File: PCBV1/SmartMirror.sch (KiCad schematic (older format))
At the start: 0 parts

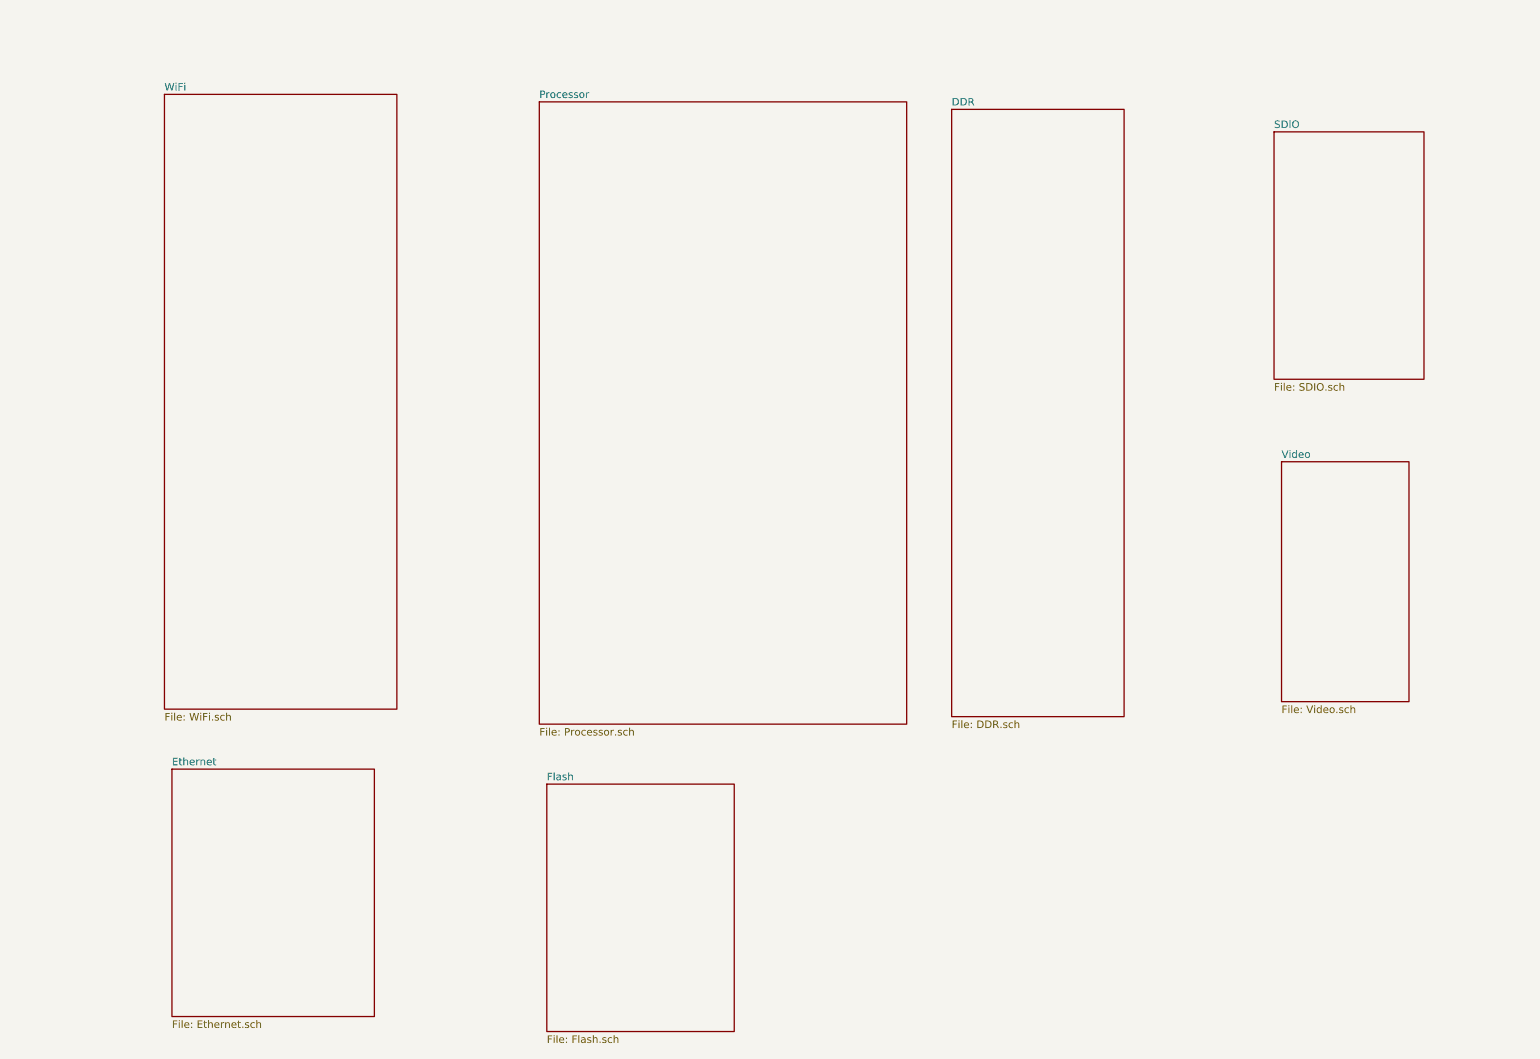
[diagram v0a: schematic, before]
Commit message: Added schematic for power through barrel jack and voltage converters, connected DRAM.
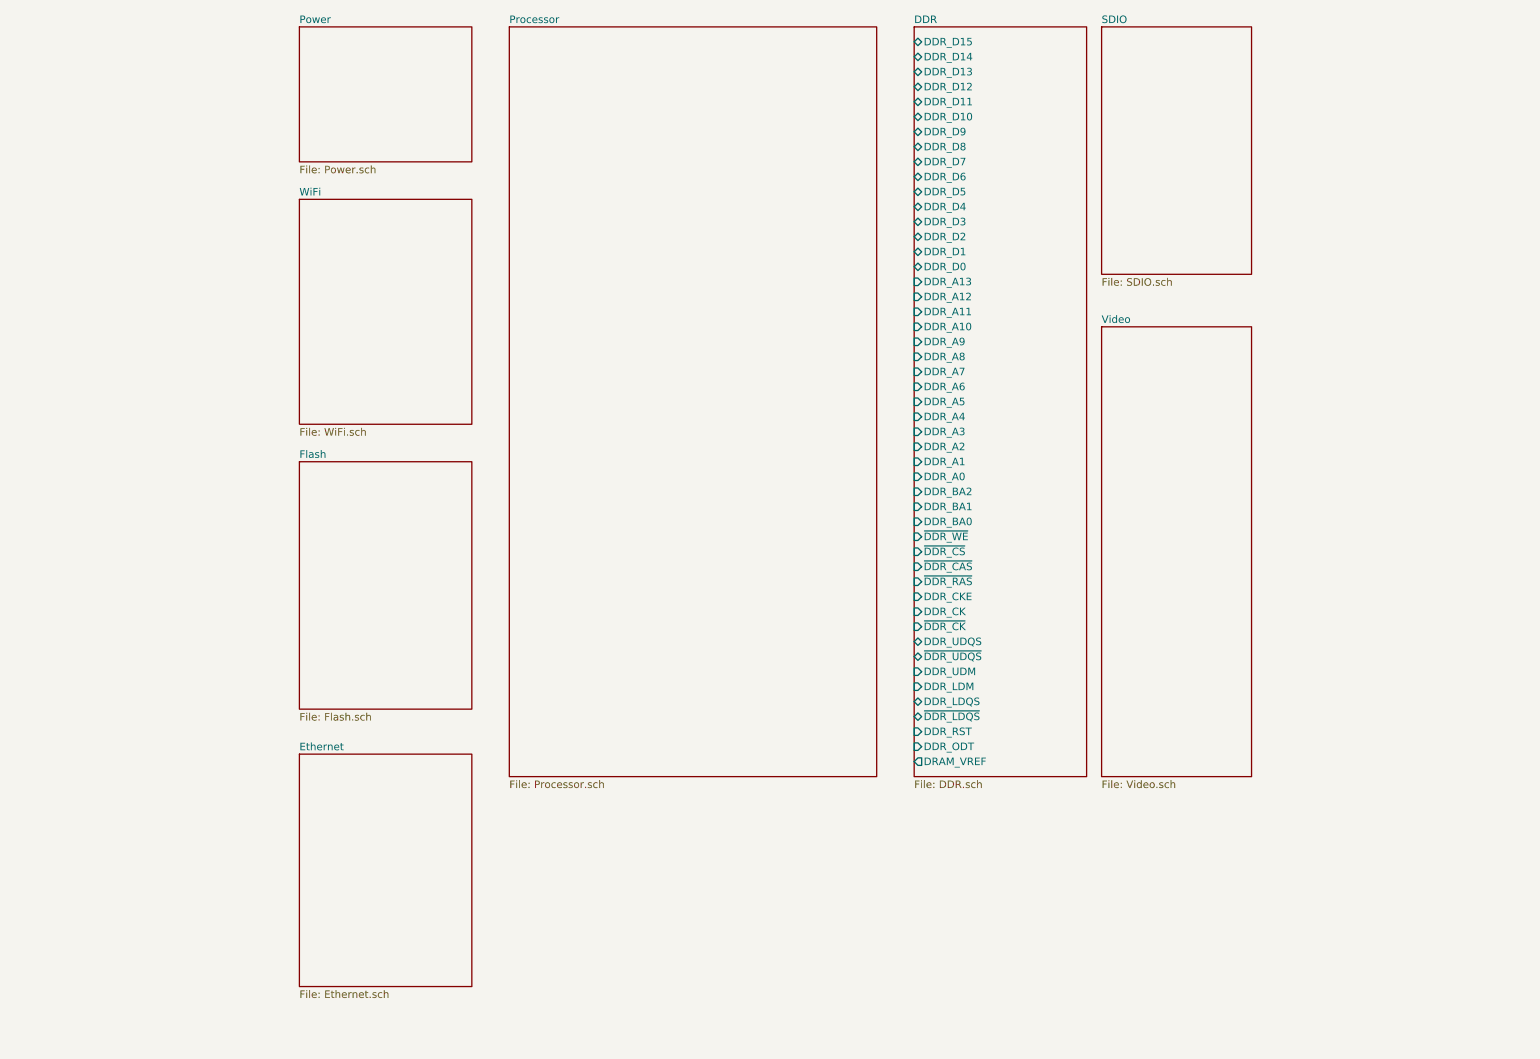
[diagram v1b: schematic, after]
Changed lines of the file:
@@
 $Descr A4 11693 8268
 encoding utf-8
-Sheet 1 8
+Sheet 1 9
 Title "Smart Mirror"
 Date "2021-01-21"
@@
 $EndDescr
 $Sheet
-S 4400 1350 2450 4150
+S 4200 850  2450 5000
 U 6009E1D9
 F0 "Processor" 50
@@
 $EndSheet
 $Sheet
-S 7150 1400 1150 4050
-U 6009E3C0
-F0 "DDR" 50
-F1 "DDR.sch" 50
-$EndSheet
-$Sheet
-S 1900 1300 1550 4100
+S 2800 2000 1150 1500
 U 6009E54D
 F0 "WiFi" 50
@@
 $EndSheet
 $Sheet
-S 1950 5800 1350 1650
+S 2800 5700 1150 1550
 U 6009E63D
 F0 "Ethernet" 50
@@
 $EndSheet
 $Sheet
-S 9300 1550 1000 1650
+S 8150 850  1000 1650
 U 6009E6CB
 F0 "SDIO" 50
@@
 $EndSheet
 $Sheet
-S 9350 3750 850  1600
+S 8150 2850 1000 3000
 U 6009E791
 F0 "Video" 50
@@
 $EndSheet
 $Sheet
-S 4450 5900 1250 1650
+S 2800 3750 1150 1650
 U 6009E7FD
 F0 "Flash" 50
 F1 "Flash.sch" 50
 $EndSheet
+$Sheet
+S 2800 850  1150 900
+U 60251FB2
+F0 "Power" 50
+F1 "Power.sch" 50
+$EndSheet
+$Sheet
+S 6900 850  1150 5000
+U 6009E3C0
+F0 "DDR" 50
+F1 "DDR.sch" 50
+F2 "DDR_D13" B L 6900 1150 50
+F3 "DDR_D15" B L 6900 950 50
+F4 "DDR_D12" B L 6900 1250 50
+F5 "DDR_D14" B L 6900 1050 50
+F6 "DDR_D11" B L 6900 1350 50
+F7 "DDR_D9" B L 6900 1550 50
+F8 "DDR_D10" B L 6900 1450 50
+F9 "DDR_D8" B L 6900 1650 50
+F10 "DDR_D0" B L 6900 2450 50
+F11 "DDR_D2" B L 6900 2250 50
+F12 "DDR_D1" B L 6900 2350 50
+F13 "DDR_D3" B L 6900 2150 50
+F14 "DDR_D6" B L 6900 1850 50
+F15 "DDR_D4" B L 6900 2050 50
+F16 "DDR_D7" B L 6900 1750 50
+F17 "DDR_D5" B L 6900 1950 50
+F18 "DDR_A8" I L 6900 3050 50
+F19 "DDR_A13" I L 6900 2550 50
+F20 "DDR_A6" I L 6900 3250 50
+F21 "DDR_A11" I L 6900 2750 50
+F22 "DDR_A9" I L 6900 2950 50
+F23 "DDR_A7" I L 6900 3150 50
+F24 "DDR_A4" I L 6900 3450 50
+F25 "DDR_A1" I L 6900 3750 50
+F26 "DDR_A2" I L 6900 3650 50
+F27 "DDR_A5" I L 6900 3350 50
+F28 "DDR_A0" I L 6900 3850 50
+F29 "DDR_A3" I L 6900 3550 50
+F30 "DDR_A12" I L 6900 2650 50
+F31 "DDR_A10" I L 6900 2850 50
+F32 "DDR_BA1" I L 6900 4050 50
+F33 "DDR_BA2" I L 6900 3950 50
+F34 "DDR_BA0" I L 6900 4150 50
+F35 "~DDR_WE" I L 6900 4250 50
+F36 "~DDR_CS" I L 6900 4350 50
+F37 "DDR_CKE" I L 6900 4650 50
+F38 "~DDR_CK" I L 6900 4850 50
+F39 "~DDR_CAS" I L 6900 4450 50
+F40 "DDR_CK" I L 6900 4750 50
+F41 "~DDR_RAS" I L 6900 4550 50
+F42 "~DDR_UDQS" B L 6900 5050 50
+F43 "DDR_UDQS" B L 6900 4950 50
+F44 "DDR_UDM" I L 6900 5150 50
+F45 "DDR_LDM" I L 6900 5250 50
+F46 "DDR_LDQS" B L 6900 5350 50
+F47 "~DDR_LDQS" B L 6900 5450 50
+F48 "DDR_RST" I L 6900 5550 50
+F49 "DDR_ODT" I L 6900 5650 50
+F50 "DRAM_VREF" O L 6900 5750 50
+$EndSheet
 $EndSCHEMATC

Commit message: Made comments and some circuits.
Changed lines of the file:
@@
 $Descr A4 11693 8268
 encoding utf-8
-Sheet 1 9
+Sheet 1 8
 Title "Smart Mirror"
 Date "2021-01-21"
@@
 $EndSheet
 $Sheet
-S 2800 5700 1150 1550
-U 6009E63D
-F0 "Ethernet" 50
-F1 "Ethernet.sch" 50
-$EndSheet
-$Sheet

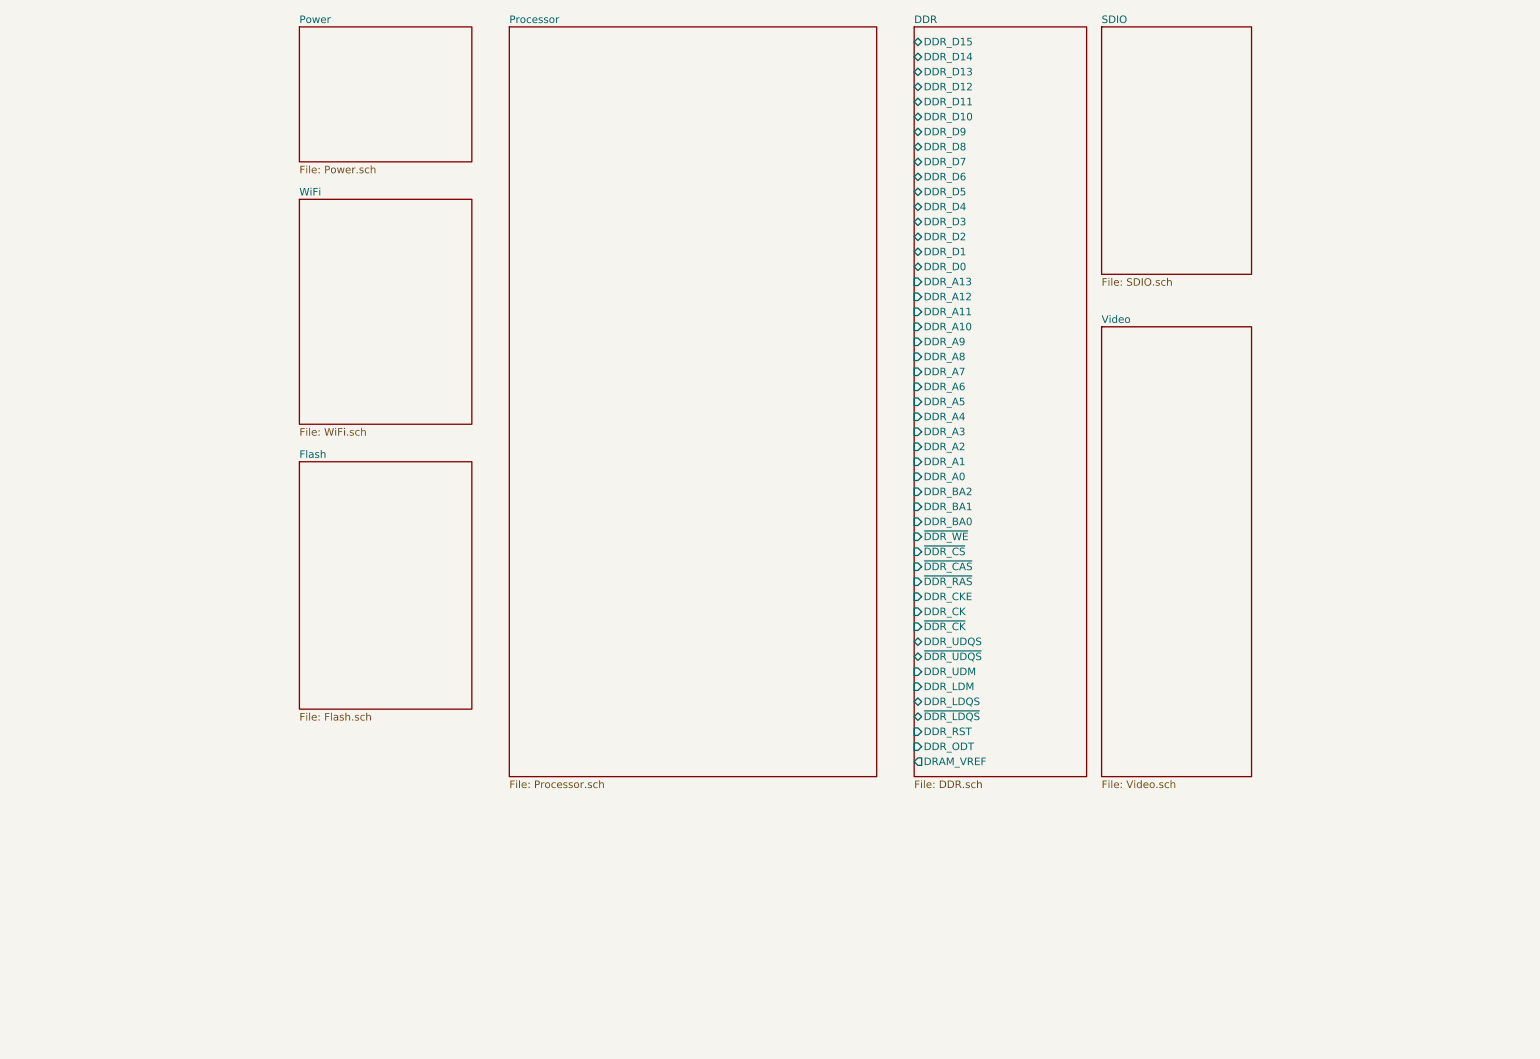
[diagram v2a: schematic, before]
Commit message: Merge of recent changes to default master (#2)
* Made a bunch of very small changes.

* Added UART, modifications to video etc.

* Minor adjustments with video connections.

* Finished video signals, added HDMI and SD connectors.
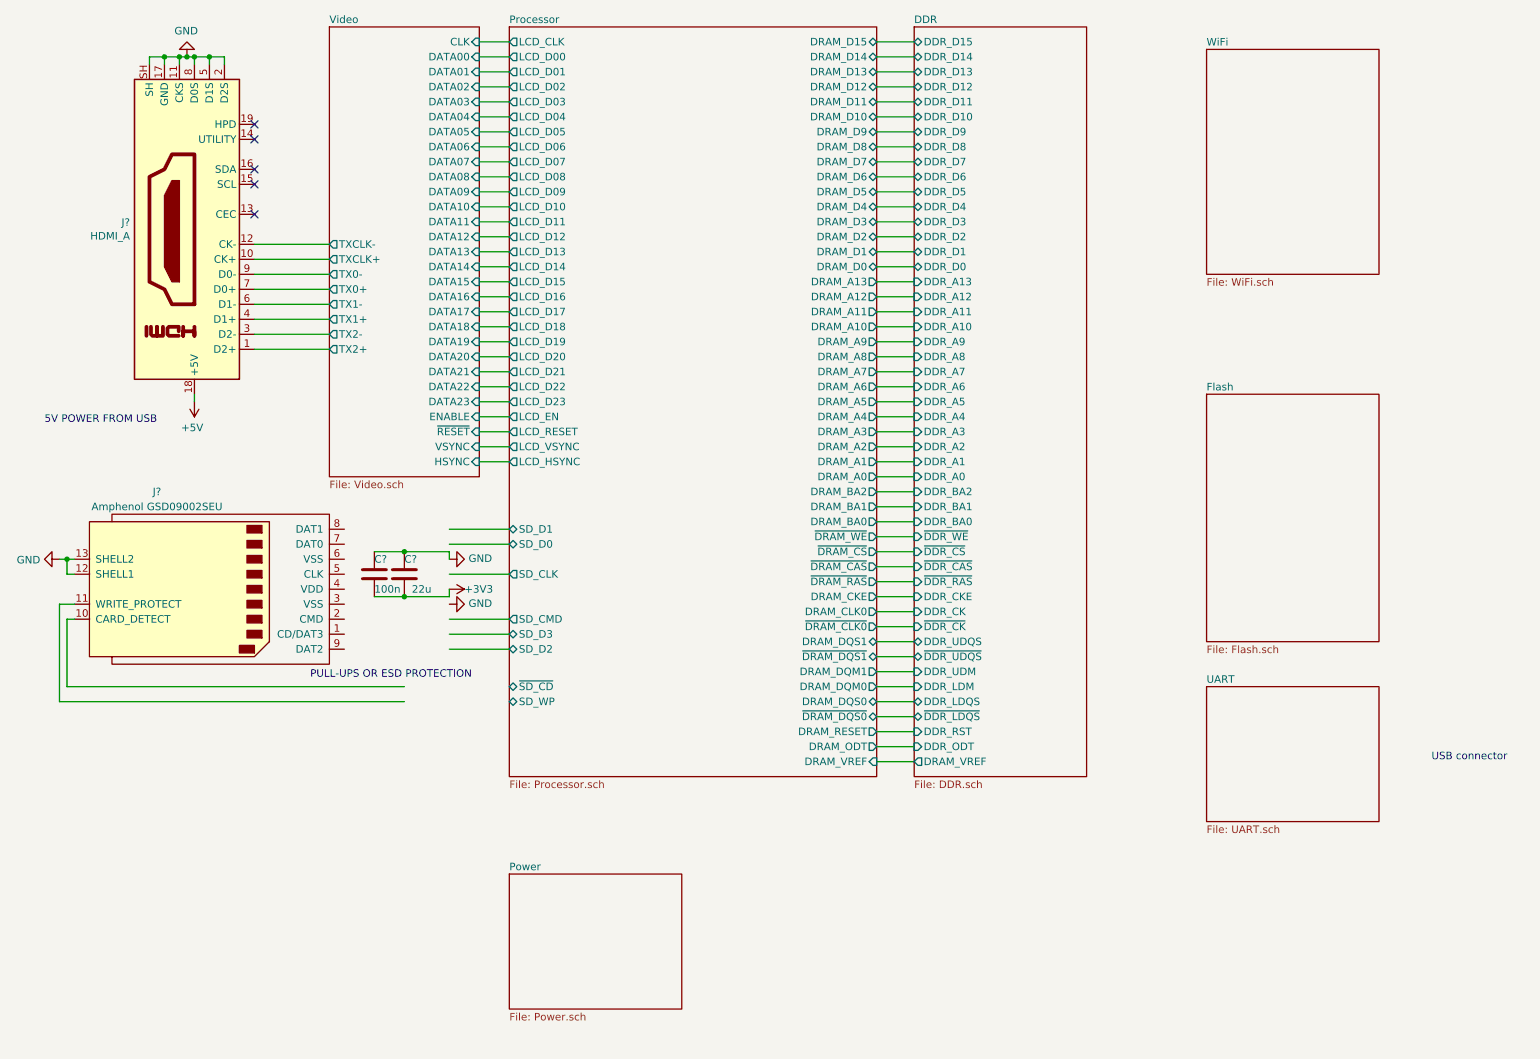
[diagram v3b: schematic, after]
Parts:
- added C?: 100n, Capacitor_SMD:C_0603_1608Metric, symbol Device:C
- added C?: 22u, Capacitor_SMD:C_0603_1608Metric, symbol Device:C
- added J?: HDMI_A, symbol Connector:HDMI_A
- added J?: Amphenol GSD09002SEU, Personal_Misc:GSD09002SEU, symbol Connector:SD_Card
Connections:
- net labels added: +3V3, +5V, GND
- wire segments 0 -> 121
- no-connect marks 0 -> 5
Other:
- note added: "5V POWER FROM USB"
- note added: "PULL-UPS OR ESD PROTECTION"
- note added: "USB connector"
